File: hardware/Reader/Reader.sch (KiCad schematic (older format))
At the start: 0 parts

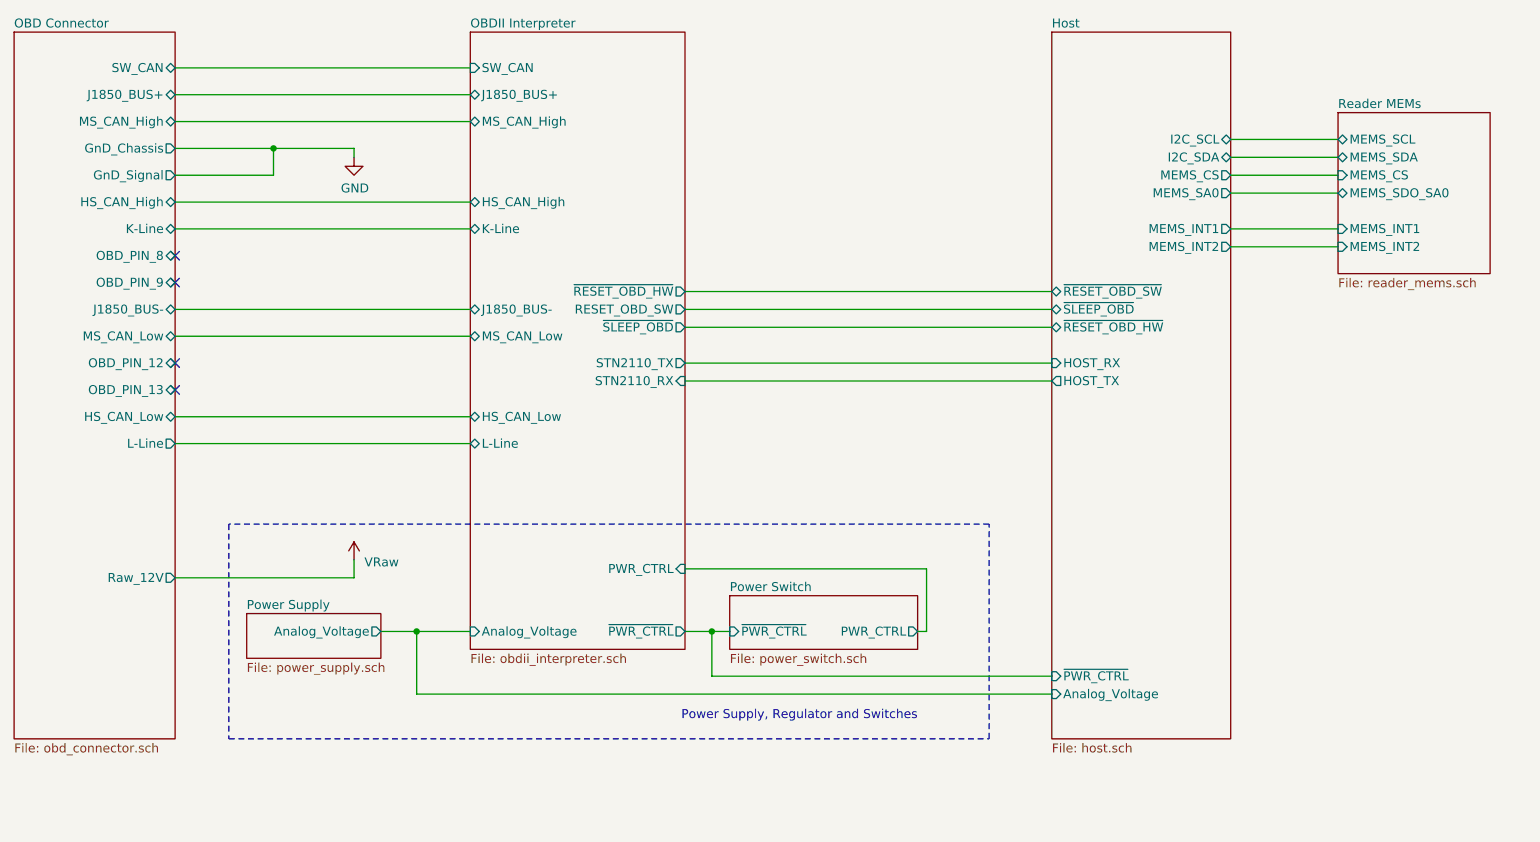
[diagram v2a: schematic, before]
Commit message: Updated reader schematic to v0.0.5 by adding ESP32, removing unused transceivers, fixed design flaws, increased header pins and fixed footprints. Working on reader PCB design
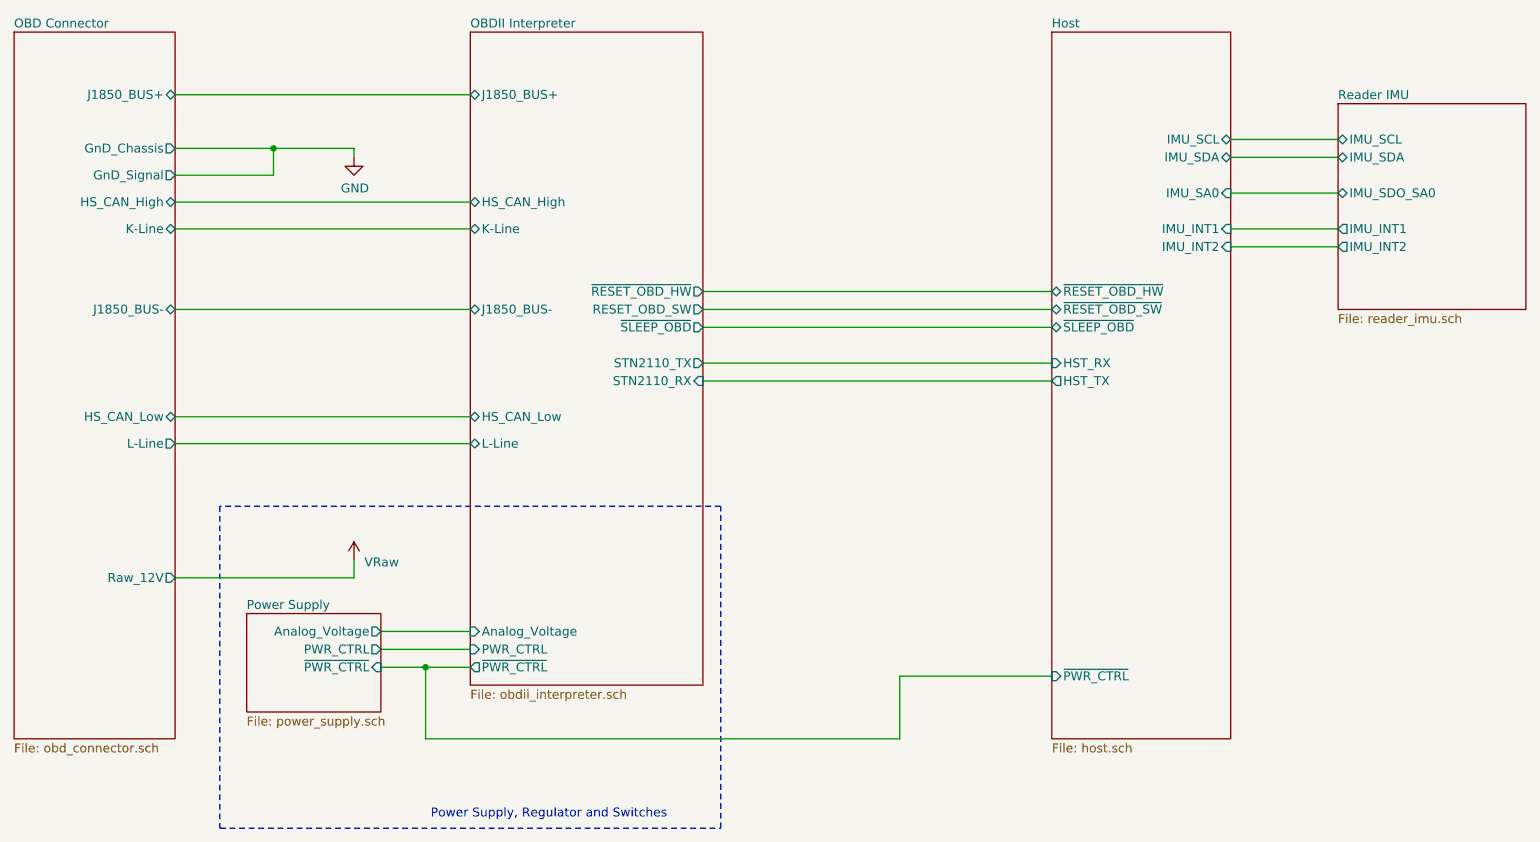
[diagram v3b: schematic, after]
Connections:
- no-connect marks 4 -> 0
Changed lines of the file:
@@
 $Descr USLetter 11000 8500
 encoding utf-8
-Sheet 1 19
+Sheet 1 17
 Title "CANnect Reader"
-Date "2020-11-19"
+Date "2020-11-27"
 Rev "0.0.05"
 Comp "CANtech"
@@
 Comment2 ""
 Comment3 ""
-Comment4 ""
+Comment4 "Component Identifier: "
 $EndDescr
-$Sheet
-S 4700 4350 1050 300
-U 5FA56A4E
-F0 "Power Switch" 50
-F1 "power_switch.sch" 50
-F2 "~PWR_CTRL~" I L 4700 4550 50
-F3 "PWR_CTRL" O R 5750 4550 50
-$EndSheet
 $Comp
 L CANtech:VRaw #V01
@@
 Wire Wire Line
 	2600 4250 2600 4150
-Wire Wire Line
-	2750 4550 2950 4550
-$Sheet
-S 3250 1200 1200 3450
-U 5F95F80B
-F0 "OBDII Interpreter" 50
-F1 "obdii_interpreter.sch" 50
-F2 "K-Line" B L 3250 2300 50
-F3 "L-Line" B L 3250 3500 50
-F4 "SW_CAN" I L 3250 1400 50
-F5 "J1850_BUS+" B L 3250 1550 50
-F6 "J1850_BUS-" B L 3250 2750 50
-F7 "MS_CAN_High" B L 3250 1700 50
-F8 "MS_CAN_Low" B L 3250 2900 50
-F9 "STN2110_TX" O R 4450 3050 50
-F10 "HS_CAN_High" B L 3250 2150 50
-F11 "HS_CAN_Low" B L 3250 3350 50
-F12 "STN2110_RX" I R 4450 3150 50
-F13 "~PWR_CTRL~" O R 4450 4550 50
-F14 "Analog_Voltage" I L 3250 4550 50
-F15 "~SLEEP_OBD~" O R 4450 2850 50
-F16 "RESET_OBD_SW" O R 4450 2750 50
-F17 "~RESET_OBD_HW~" O R 4450 2650 50
-F18 "PWR_CTRL" I R 4450 4200 50
-$EndSheet
-Wire Notes Line
-	1900 3950 1900 5150
-Wire Notes Line
-	1900 5150 6150 5150
-Wire Notes Line
-	6150 5150 6150 3950
-Wire Notes Line
-	6150 3950 1900 3950
-Text Notes 5750 5050 2    50   ~ 0
+Text Notes 4350 5600 2    50   ~ 0
 Power Supply, Regulator and Switches
-$Sheet
-S 700  1200 900  3950
-U 5FF6FE24
-F0 "OBD Connector" 50
-F1 "obd_connector.sch" 50
-F2 "SW_CAN" B R 1600 1400 50
-F3 "Raw_12V" O R 1600 4250 50
-F4 "J1850_BUS+" B R 1600 1550 50
-F5 "MS_CAN_High" B R 1600 1700 50
-F6 "GnD_Chassis" O R 1600 1850 50
-F7 "GnD_Signal" O R 1600 2000 50
-F8 "HS_CAN_High" B R 1600 2150 50
-F9 "K-Line" B R 1600 2300 50
-F10 "OBD_PIN_8" B R 1600 2450 50
-F11 "OBD_PIN_9" B R 1600 2600 50
-F12 "MS_CAN_Low" B R 1600 2900 50
-F13 "OBD_PIN_12" B R 1600 3050 50
-F14 "OBD_PIN_13" B R 1600 3200 50
-F15 "HS_CAN_Low" B R 1600 3350 50
-F16 "L-Line" O R 1600 3500 50
-F17 "J1850_BUS-" B R 1600 2750 50
-$EndSheet
 Wire Wire Line
 	1600 4250 2600 4250
 Wire Wire Line
-	1600 1400 3250 1400
-Wire Wire Line
 	1600 1550 3250 1550
-Wire Wire Line
-	3250 1700 1600 1700
 $Comp
 L power:GND #PWR01
@@
 	1600 2750 3250 2750
 Wire Wire Line
-	3250 2900 1600 2900
-Wire Wire Line
 	3250 3500 1600 3500
-NoConn ~ 1600 2450
-NoConn ~ 1600 2600
-NoConn ~ 1600 3050
-NoConn ~ 1600 3200
-Wire Wire Line
-	4450 4550 4600 4550
-Wire Wire Line
-	5750 4550 5800 4550
-Wire Wire Line
-	5800 4550 5800 4200
-Wire Wire Line
-	5800 4200 4450 4200
 Wire Wire Line
 	1600 3350 3250 3350
-Wire Wire Line
-	6500 2650 4450 2650
-Wire Wire Line
-	4450 2750 6500 2750
-Wire Wire Line
-	6500 2850 4450 2850
-Wire Wire Line
-	6500 3150 4450 3150
-Wire Wire Line
-	4450 3050 6500 3050
-Wire Wire Line
-	2950 4900 6500 4900
-Connection ~ 2950 4550
-Wire Wire Line
-	2950 4550 3250 4550
-Wire Wire Line
-	4600 4550 4600 4800
-Wire Wire Line
-	4600 4800 6500 4800
-Connection ~ 4600 4550
-Wire Wire Line
-	4600 4550 4700 4550
 $Sheet
 S 6500 1200 1000 3950
@@
 F0 "Host" 50
 F1 "host.sch" 50
-F2 "HOST_RX" I L 6500 3050 50
-F3 "HOST_TX" O L 6500 3150 50
-F4 "I2C_SCL" B R 7500 1800 50
-F5 "I2C_SDA" B R 7500 1900 50
-F6 "~SLEEP_OBD~" B L 6500 2750 50
-F7 "~RESET_OBD_SW~" B L 6500 2650 50
-F8 "~RESET_OBD_HW~" B L 6500 2850 50
-F9 "MEMS_CS" O R 7500 2000 50
-F10 "MEMS_SA0" O R 7500 2100 50
-F11 "Analog_Voltage" I L 6500 4900 50
-F12 "~PWR_CTRL~" I L 6500 4800 50
-F13 "MEMS_INT2" O R 7500 2400 50
-F14 "MEMS_INT1" O R 7500 2300 50
+F2 "~SLEEP_OBD~" B L 6500 2850 50
+F3 "~RESET_OBD_SW~" B L 6500 2750 50
+F4 "~RESET_OBD_HW~" B L 6500 2650 50
+F5 "~PWR_CTRL~" I L 6500 4800 50
+F6 "IMU_INT1" I R 7500 2300 50
+F7 "IMU_SA0" I R 7500 2100 50
+F8 "IMU_INT2" I R 7500 2400 50
+F9 "IMU_SDA" B R 7500 1900 50
+F10 "IMU_SCL" B R 7500 1800 50
+F11 "HST_RX" I L 6500 3050 50
+F12 "HST_TX" O L 6500 3150 50
 $EndSheet
 Wire Wire Line
@@
 	7500 2100 8100 2100
 Wire Wire Line
-	7500 2000 8100 2000
-Wire Wire Line
 	7500 1900 8100 1900
 Wire Wire Line
 	7500 1800 8100 1800
 $Sheet
-S 8100 1650 850  900
-U 5F988046
-F0 "Reader MEMs" 50
-F1 "reader_mems.sch" 50
-F2 "MEMS_SCL" B L 8100 1800 50
-F3 "MEMS_SDA" B L 8100 1900 50
-F4 "MEMS_INT1" I L 8100 2300 50
-F5 "MEMS_CS" I L 8100 2000 50
-F6 "MEMS_SDO_SA0" B L 8100 2100 50
-F7 "MEMS_INT2" I L 8100 2400 50
-$EndSheet
-Wire Wire Line
-	2950 4550 2950 4900
-$Sheet
-S 2000 4450 750  250
+S 2000 4450 750  550
 U 5F8ADA45
 F0 "Power Supply" 50
 F1 "power_supply.sch" 50
 F2 "Analog_Voltage" O R 2750 4550 50
+F3 "~PWR_CTRL~" I R 2750 4750 50
+F4 "PWR_CTRL" O R 2750 4650 50
+$EndSheet
+$Sheet
+S 8100 1600 1050 1150
+U 5FC2797A
+F0 "Reader IMU" 50
+F1 "reader_imu.sch" 50
+F2 "IMU_SCL" B L 8100 1800 50
+F3 "IMU_SDA" B L 8100 1900 50
+F4 "IMU_INT1" O L 8100 2300 50
+F5 "IMU_SDO_SA0" B L 8100 2100 50
+F6 "IMU_INT2" O L 8100 2400 50
+$EndSheet
+Wire Wire Line
+	2750 4550 3250 4550
+Wire Wire Line
+	2750 4650 3250 4650
+Wire Wire Line
+	3250 4750 3000 4750
+Wire Wire Line
+	3000 5150 5650 5150
+Wire Wire Line
+	5650 5150 5650 4800
+Wire Wire Line
+	5650 4800 6500 4800
+Wire Wire Line
+	3000 4750 3000 5150
+Connection ~ 3000 4750
+Wire Wire Line
+	3000 4750 2750 4750
+Wire Notes Line
+	1850 3850 1850 5650
+Wire Notes Line
+	1850 5650 4650 5650
+Wire Notes Line
+	4650 5650 4650 3850
+Wire Notes Line
+	4650 3850 1850 3850
+Wire Wire Line
+	4550 2650 6500 2650
+Wire Wire Line
+	6500 2750 4550 2750
+Wire Wire Line
+	4550 2850 6500 2850
+Wire Wire Line
+	6500 3050 4550 3050
+Wire Wire Line
+	6500 3150 4550 3150
+$Sheet
+S 700  1200 900  3950
+U 5FF6FE24
+F0 "OBD Connector" 50
+F1 "obd_connector.sch" 50
+F2 "Raw_12V" O R 1600 4250 50
+F3 "J1850_BUS+" B R 1600 1550 50
+F4 "GnD_Chassis" O R 1600 1850 50
+F5 "GnD_Signal" O R 1600 2000 50
+F6 "HS_CAN_High" B R 1600 2150 50
+F7 "K-Line" B R 1600 2300 50
+F8 "HS_CAN_Low" B R 1600 3350 50
+F9 "L-Line" O R 1600 3500 50
+F10 "J1850_BUS-" B R 1600 2750 50
+$EndSheet
+$Sheet
+S 3250 1200 1300 3650
+U 5F95F80B
+F0 "OBDII Interpreter" 50
+F1 "obdii_interpreter.sch" 50
+F2 "K-Line" B L 3250 2300 50
+F3 "L-Line" B L 3250 3500 50
+F4 "J1850_BUS+" B L 3250 1550 50
+F5 "J1850_BUS-" B L 3250 2750 50
+F6 "STN2110_TX" O R 4550 3050 50
+F7 "HS_CAN_High" B L 3250 2150 50
+F8 "HS_CAN_Low" B L 3250 3350 50
+F9 "STN2110_RX" I R 4550 3150 50
+F10 "~PWR_CTRL~" O L 3250 4750 50
+F11 "Analog_Voltage" I L 3250 4550 50
+F12 "~SLEEP_OBD~" O R 4550 2850 50
+F13 "RESET_OBD_SW" O R 4550 2750 50
+F14 "~RESET_OBD_HW~" O R 4550 2650 50
+F15 "PWR_CTRL" I L 3250 4650 50
 $EndSheet
 $EndSCHEMATC

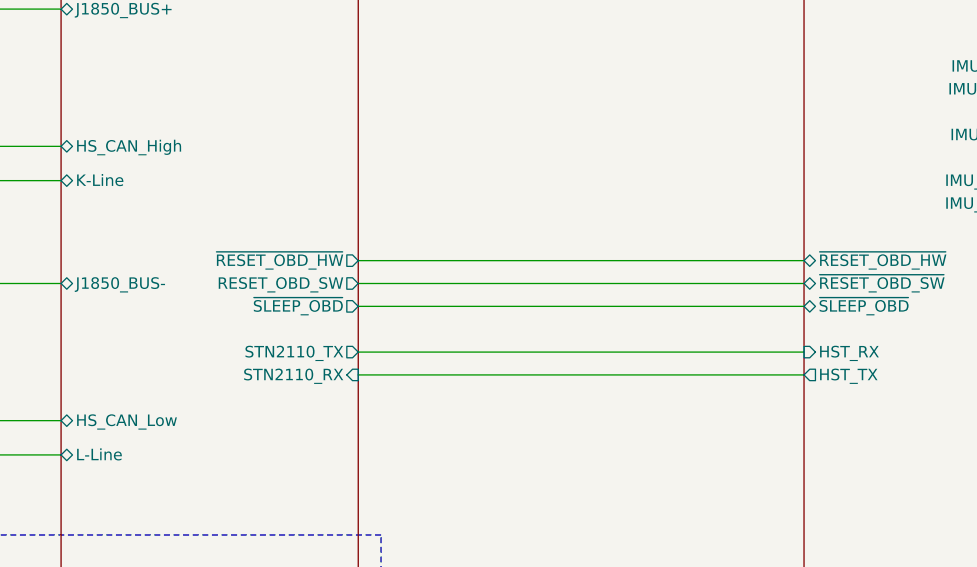
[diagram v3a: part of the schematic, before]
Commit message: Updated schematic and gerber to v0.0.05. Added ESP32. Removed MS CAN and SW CAN Transceivers. Added silkscreen text to header pins. Improved readability
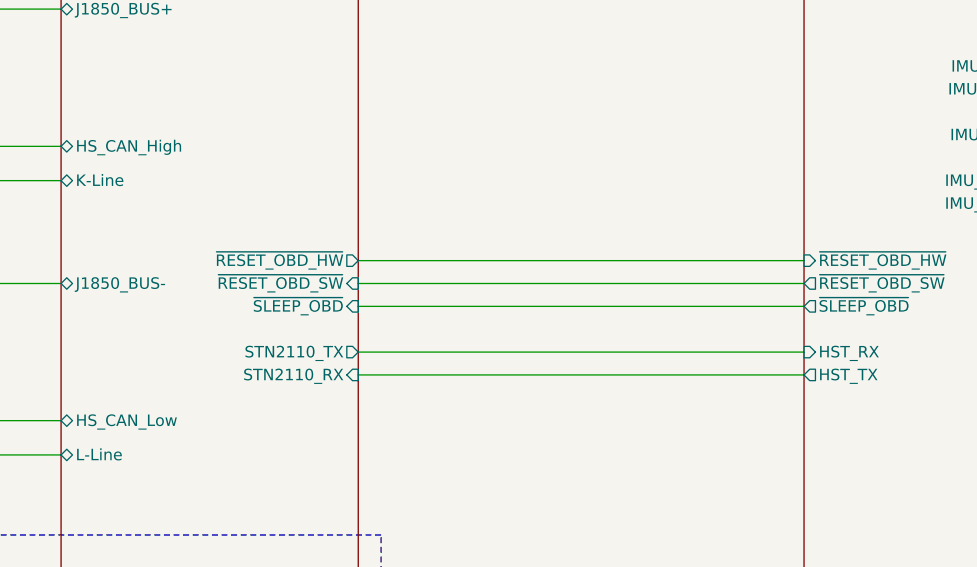
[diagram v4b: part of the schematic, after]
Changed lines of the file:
@@
 Sheet 1 17
 Title "CANnect Reader"
-Date "2020-11-27"
+Date "2020-11-29"
 Rev "0.0.05"
 Comp "CANtech"
@@
 Wire Wire Line
 	1600 3350 3250 3350
-$Sheet
-S 6500 1200 1000 3950
-U 5F91C7D3
-F0 "Host" 50
-F1 "host.sch" 50
-F2 "~SLEEP_OBD~" B L 6500 2850 50
-F3 "~RESET_OBD_SW~" B L 6500 2750 50
-F4 "~RESET_OBD_HW~" B L 6500 2650 50
-F5 "~PWR_CTRL~" I L 6500 4800 50
-F6 "IMU_INT1" I R 7500 2300 50
-F7 "IMU_SA0" I R 7500 2100 50
-F8 "IMU_INT2" I R 7500 2400 50
-F9 "IMU_SDA" B R 7500 1900 50
-F10 "IMU_SCL" B R 7500 1800 50
-F11 "HST_RX" I L 6500 3050 50
-F12 "HST_TX" O L 6500 3150 50
-$EndSheet
 Wire Wire Line
 	8100 2400 7500 2400
 Wire Wire Line
 	7500 2300 8100 2300
-Wire Wire Line
-	7500 2100 8100 2100
 Wire Wire Line
 	7500 1900 8100 1900
@@
 F3 "~PWR_CTRL~" I R 2750 4750 50
 F4 "PWR_CTRL" O R 2750 4650 50
-$EndSheet
-$Sheet
-S 8100 1600 1050 1150
-U 5FC2797A
-F0 "Reader IMU" 50
-F1 "reader_imu.sch" 50
-F2 "IMU_SCL" B L 8100 1800 50
-F3 "IMU_SDA" B L 8100 1900 50
-F4 "IMU_INT1" O L 8100 2300 50
-F5 "IMU_SDO_SA0" B L 8100 2100 50
-F6 "IMU_INT2" O L 8100 2400 50
 $EndSheet
 Wire Wire Line
@@
 F10 "J1850_BUS-" B R 1600 2750 50
 $EndSheet
+Wire Wire Line
+	7500 2100 8100 2100
+$Sheet
+S 6500 1200 1000 3950
+U 5F91C7D3
+F0 "Host" 50
+F1 "host.sch" 50
+F2 "~PWR_CTRL~" I L 6500 4800 50
+F3 "IMU_INT1" I R 7500 2300 50
+F4 "IMU_SA0" I R 7500 2100 50
+F5 "IMU_INT2" I R 7500 2400 50
+F6 "IMU_SDA" B R 7500 1900 50
+F7 "IMU_SCL" B R 7500 1800 50
+F8 "HST_RX" I L 6500 3050 50
+F9 "HST_TX" O L 6500 3150 50
+F10 "~RESET_OBD_HW~" I L 6500 2650 50
+F11 "~RESET_OBD_SW~" O L 6500 2750 50
+F12 "~SLEEP_OBD~" O L 6500 2850 50
+$EndSheet
+$Sheet
+S 8100 1600 1050 1150
+U 5FC2797A
+F0 "Reader IMU" 50
+F1 "reader_imu.sch" 50
+F2 "IMU_SCL" B L 8100 1800 50
+F3 "IMU_SDA" B L 8100 1900 50
+F4 "IMU_INT1" O L 8100 2300 50
+F5 "IMU_SDO_SA0" B L 8100 2100 50
+F6 "IMU_INT2" O L 8100 2400 50
+$EndSheet
 $Sheet
 S 3250 1200 1300 3650
@@
 F10 "~PWR_CTRL~" O L 3250 4750 50
 F11 "Analog_Voltage" I L 3250 4550 50
-F12 "~SLEEP_OBD~" O R 4550 2850 50
-F13 "RESET_OBD_SW" O R 4550 2750 50
-F14 "~RESET_OBD_HW~" O R 4550 2650 50
-F15 "PWR_CTRL" I L 3250 4650 50
+F12 "~RESET_OBD_HW~" O R 4550 2650 50
+F13 "PWR_CTRL" I L 3250 4650 50
+F14 "~RESET_OBD_SW~" I R 4550 2750 50
+F15 "~SLEEP_OBD~" I R 4550 2850 50
 $EndSheet
 $EndSCHEMATC
